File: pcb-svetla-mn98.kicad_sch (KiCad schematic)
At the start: 13 parts, among them J1 Conn_01x02_Pin, J10 Conn_01x02_Pin, J11 Conn_01x02_Pin, J12 Conn_01x02_Pin, J13 Conn_01x08_Socket, J2 Conn_01x02_Pin, J3 Conn_01x02_Pin, J4 Conn_01x02_Pin, J5 Conn_01x02_Pin, J6 Conn_01x02_Pin, J7 Conn_01x02_Pin, J8 Conn_01x02_Pin, J9 Conn_01x02_Pin

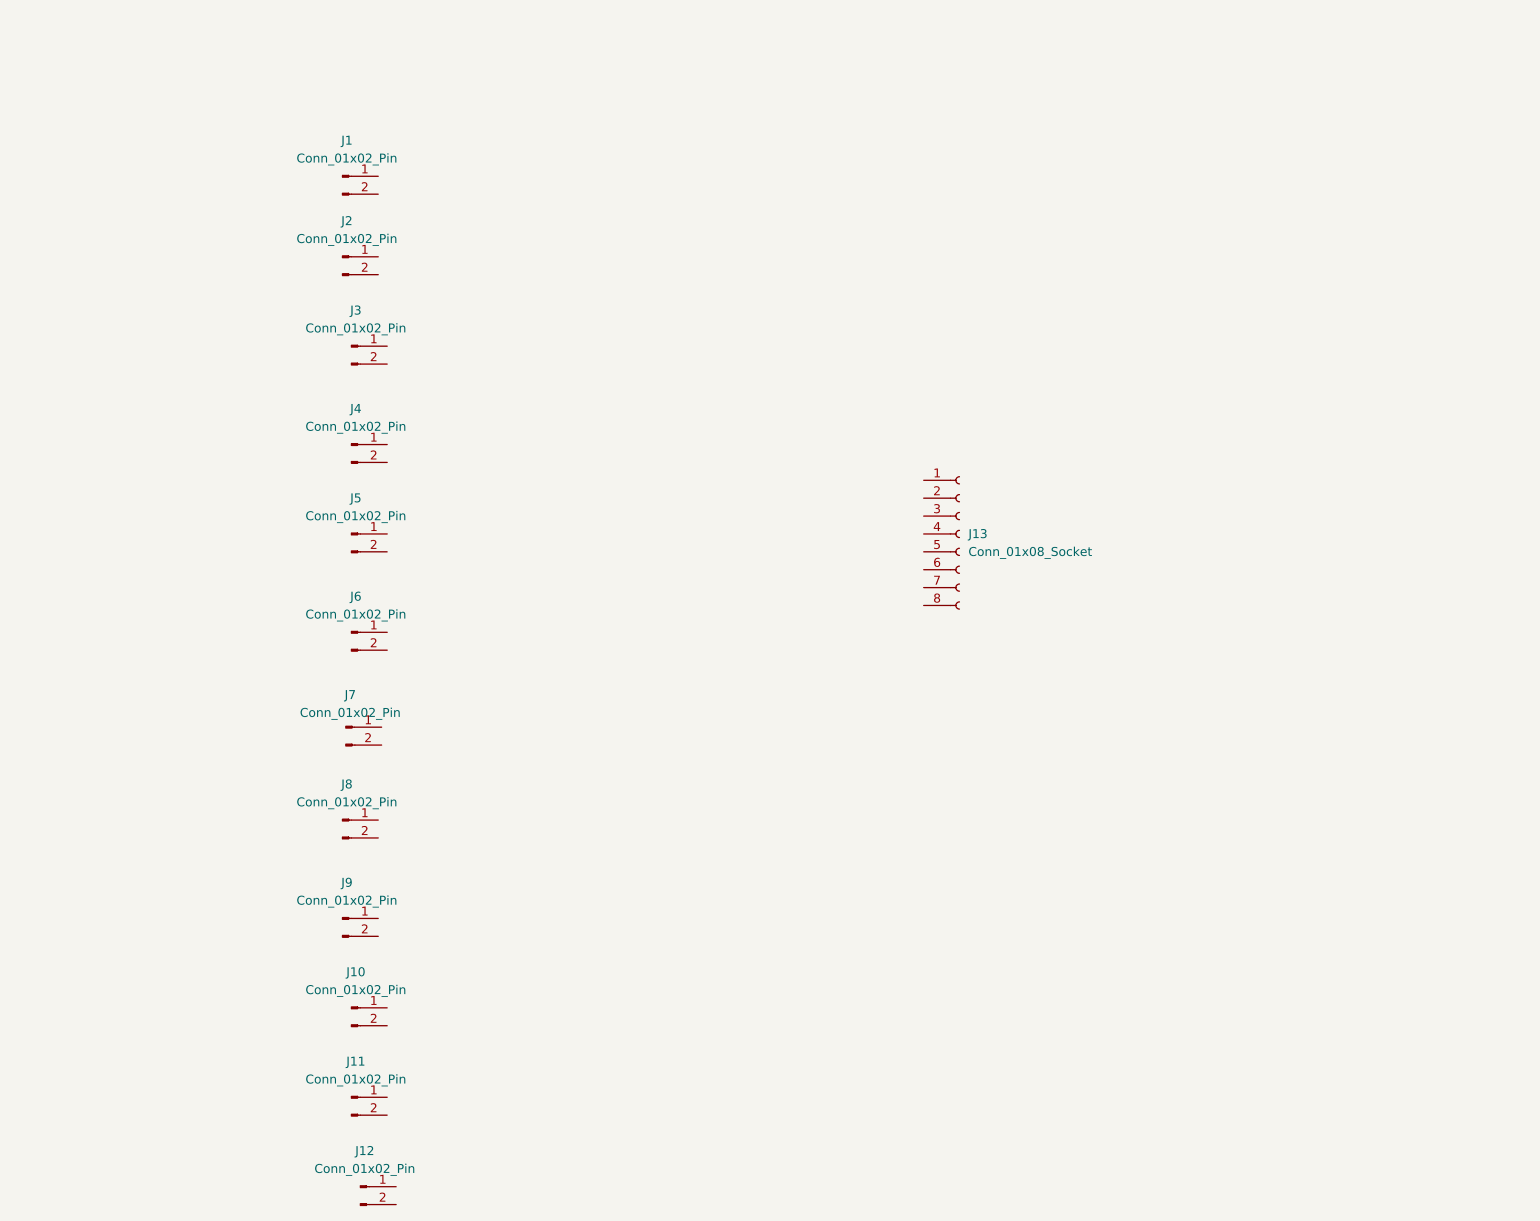
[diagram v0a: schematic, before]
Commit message: Add synchronized KiCad schematic
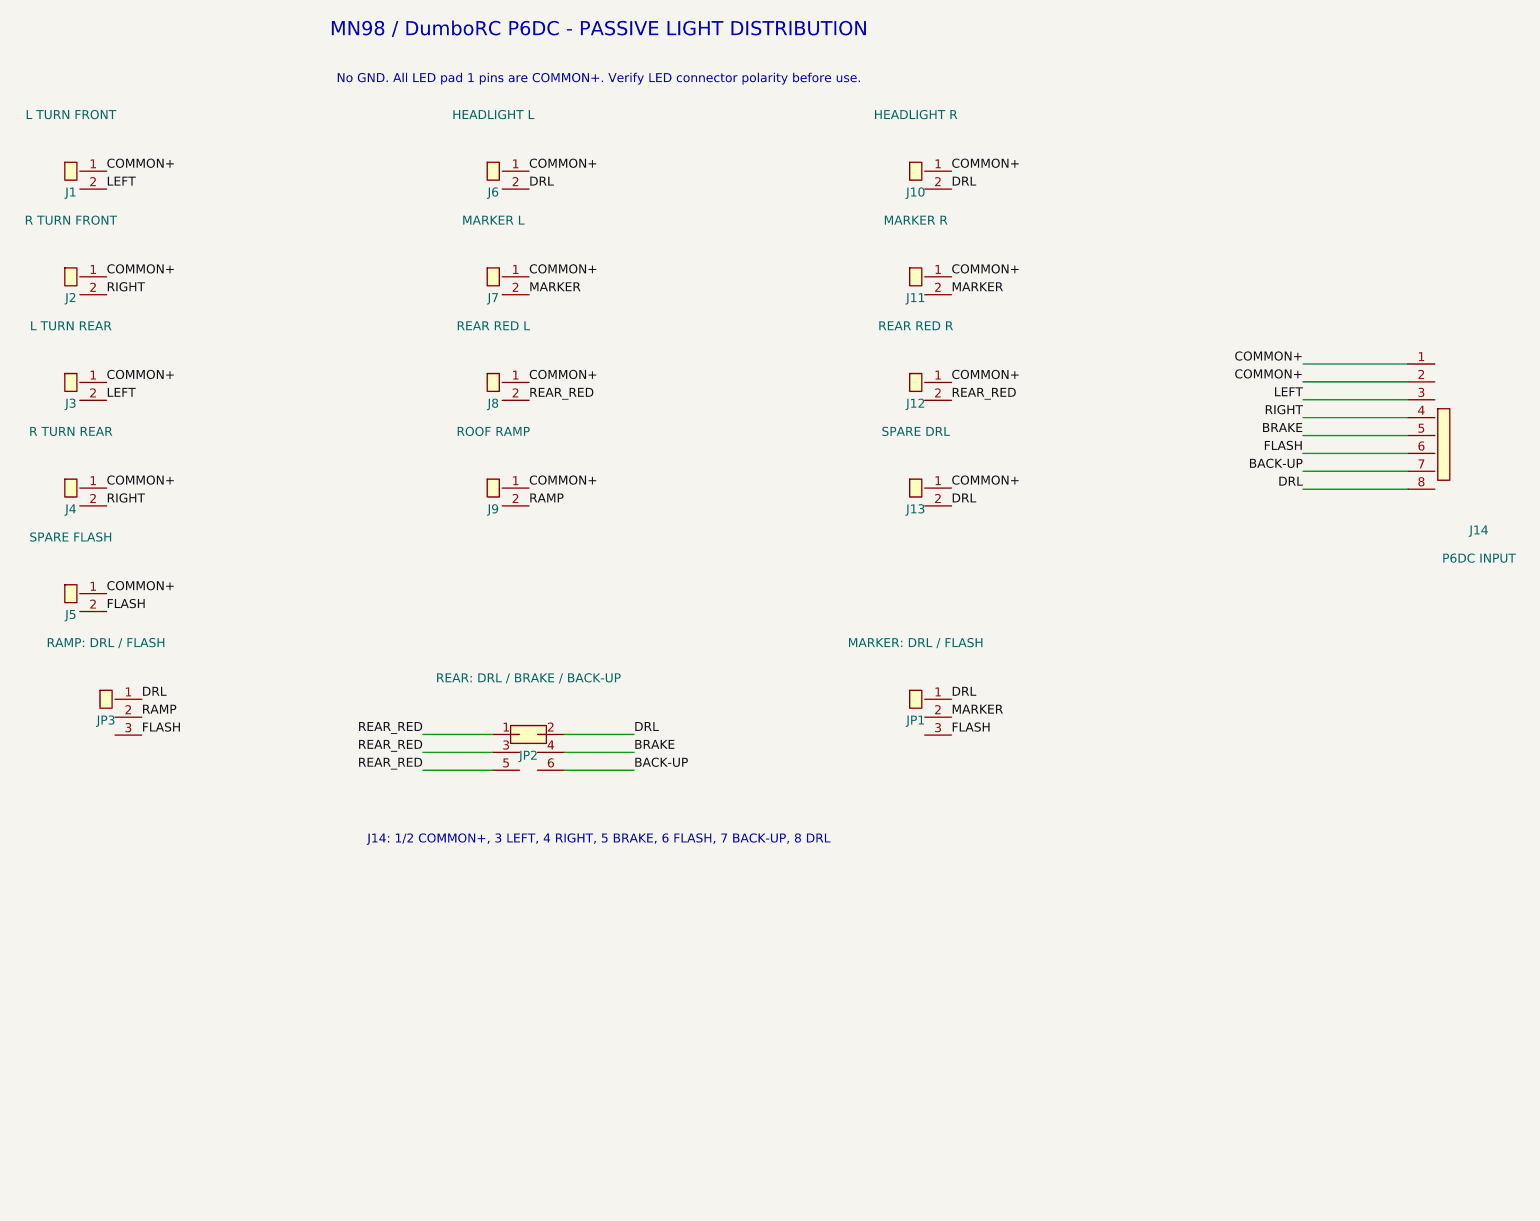
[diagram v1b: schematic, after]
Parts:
- removed J1, J10, J11, J12, J2, J3, J4, J5, J6, J7, J8, J9: Conn_01x02_Pin, Connector_JST:JST_PH_S2B-PH-K_1x02_P2.00mm_Horizontal, symbol Connector:Conn_01x02_Pin
- removed J13: Conn_01x08_Socket, Connector_JST:JST_XH_S8B-XH-A_1x08_P2.50mm_Horizontal, symbol Connector:Conn_01x08_Socket
- added J1: L TURN FRONT, Connector_JST:JST_PH_S2B-PH-K_1x02_P2.00mm_Horizontal, symbol MN98:Conn_01x02
- added J10: HEADLIGHT R, Connector_JST:JST_PH_S2B-PH-K_1x02_P2.00mm_Horizontal, symbol MN98:Conn_01x02
- added J11: MARKER R, Connector_JST:JST_PH_S2B-PH-K_1x02_P2.00mm_Horizontal, symbol MN98:Conn_01x02
- added J12: REAR RED R, Connector_JST:JST_PH_S2B-PH-K_1x02_P2.00mm_Horizontal, symbol MN98:Conn_01x02
- added J13: SPARE DRL, Connector_JST:JST_PH_S2B-PH-K_1x02_P2.00mm_Horizontal, symbol MN98:Conn_01x02
- added J14: P6DC INPUT, Connector_JST:JST_PH_S8B-PH-K_1x08_P2.00mm_Horizontal, symbol MN98:Conn_01x08
- added J2: R TURN FRONT, Connector_JST:JST_PH_S2B-PH-K_1x02_P2.00mm_Horizontal, symbol MN98:Conn_01x02
- added J3: L TURN REAR, Connector_JST:JST_PH_S2B-PH-K_1x02_P2.00mm_Horizontal, symbol MN98:Conn_01x02
- added J4: R TURN REAR, Connector_JST:JST_PH_S2B-PH-K_1x02_P2.00mm_Horizontal, symbol MN98:Conn_01x02
- added J5: SPARE FLASH, Connector_JST:JST_PH_S2B-PH-K_1x02_P2.00mm_Horizontal, symbol MN98:Conn_01x02
- added J6: HEADLIGHT L, Connector_JST:JST_PH_S2B-PH-K_1x02_P2.00mm_Horizontal, symbol MN98:Conn_01x02
- added J7: MARKER L, Connector_JST:JST_PH_S2B-PH-K_1x02_P2.00mm_Horizontal, symbol MN98:Conn_01x02
- added J8: REAR RED L, Connector_JST:JST_PH_S2B-PH-K_1x02_P2.00mm_Horizontal, symbol MN98:Conn_01x02
- added J9: ROOF RAMP, Connector_JST:JST_PH_S2B-PH-K_1x02_P2.00mm_Horizontal, symbol MN98:Conn_01x02
- added JP1: MARKER: DRL / FLASH, Connector_PinHeader_2.54mm:PinHeader_1x03_P2.54mm_Horizontal, symbol MN98:Conn_01x03
- added JP2: REAR: DRL / BRAKE / BACK-UP, Connector_PinHeader_2.54mm:PinHeader_2x03_P2.54mm_Vertical, symbol MN98:Conn_02x03
- added JP3: RAMP: DRL / FLASH, Connector_PinHeader_2.54mm:PinHeader_1x03_P2.54mm_Horizontal, symbol MN98:Conn_01x03
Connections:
- new net BACK-UP: J14.7 (Pin_7), JP2.6 (Pin_6)
- new net BRAKE: J14.5 (Pin_5), JP2.4 (Pin_4)
- new net COMMON+: J1.1 (Pin_1), J10.1 (Pin_1), J11.1 (Pin_1), J12.1 (Pin_1), J13.1 (Pin_1), J14.1 (Pin_1), J14.2 (Pin_2), J2.1 (Pin_1), J3.1 (Pin_1), J4.1 (Pin_1), J5.1 (Pin_1), J6.1 (Pin_1), J7.1 (Pin_1), J8.1 (Pin_1), J9.1 (Pin_1)
- new net DRL: J10.2 (Pin_2), J13.2 (Pin_2), J14.8 (Pin_8), J6.2 (Pin_2), JP1.1 (Pin_1), JP2.2 (Pin_2), JP3.1 (Pin_1)
- new net FLASH: J14.6 (Pin_6), J5.2 (Pin_2), JP1.3 (Pin_3), JP3.3 (Pin_3)
- new net LEFT: J1.2 (Pin_2), J14.3 (Pin_3), J3.2 (Pin_2)
- new net MARKER: J11.2 (Pin_2), J7.2 (Pin_2), JP1.2 (Pin_2)
- new net RAMP: J9.2 (Pin_2), JP3.2 (Pin_2)
- new net REAR_RED: J12.2 (Pin_2), J8.2 (Pin_2), JP2.1 (Pin_1), JP2.3 (Pin_3), JP2.5 (Pin_5)
- new net RIGHT: J14.4 (Pin_4), J2.2 (Pin_2), J4.2 (Pin_2)
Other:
- note added: "J14: 1/2 COMMON+, 3 LEFT, 4 RIGHT, 5 BRAKE, 6 FLASH, 7 BACK-UP, 8 DRL"
- note added: "MN98 / DumboRC P6DC - PASSIVE LIGHT DISTRIBUTION"
- note added: "No GND. All LED pad 1 pins are COMMON+. Verify LED connector polarity before use."
